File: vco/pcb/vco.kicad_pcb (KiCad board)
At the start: 2 copper layers, 50.5 x 108.5 mm, 98 parts, among them J1 Conn_02x05_Odd_Even, J10 AudioJack2_SwitchT, J2 AudioJack2_SwitchT, J3 AudioJack2_SwitchT, J4 AudioJack2_SwitchT, J5 AudioJack2_SwitchT, J6 AudioJack2_SwitchT, J7 AudioJack2_SwitchT, J8 AudioJack2_SwitchT, J9 AudioJack2_SwitchT, Q1 DMMT3906W, Q2 BC847, SW1 SW_SPDT, SW2 SW_SPDT, U1 TL072, U2 TL074, U3 LM13700, U4 ICM7555xB, U5 TL074

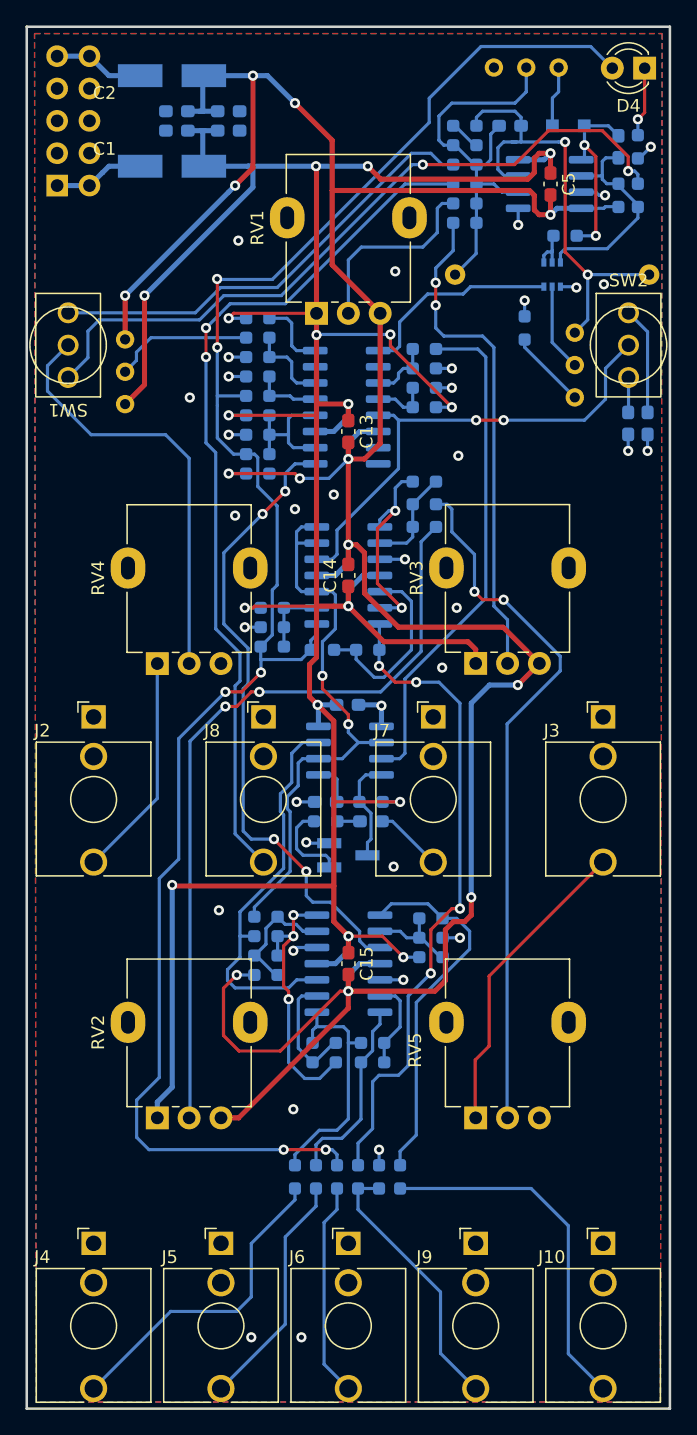
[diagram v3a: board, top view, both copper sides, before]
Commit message: vco: Organize component markings
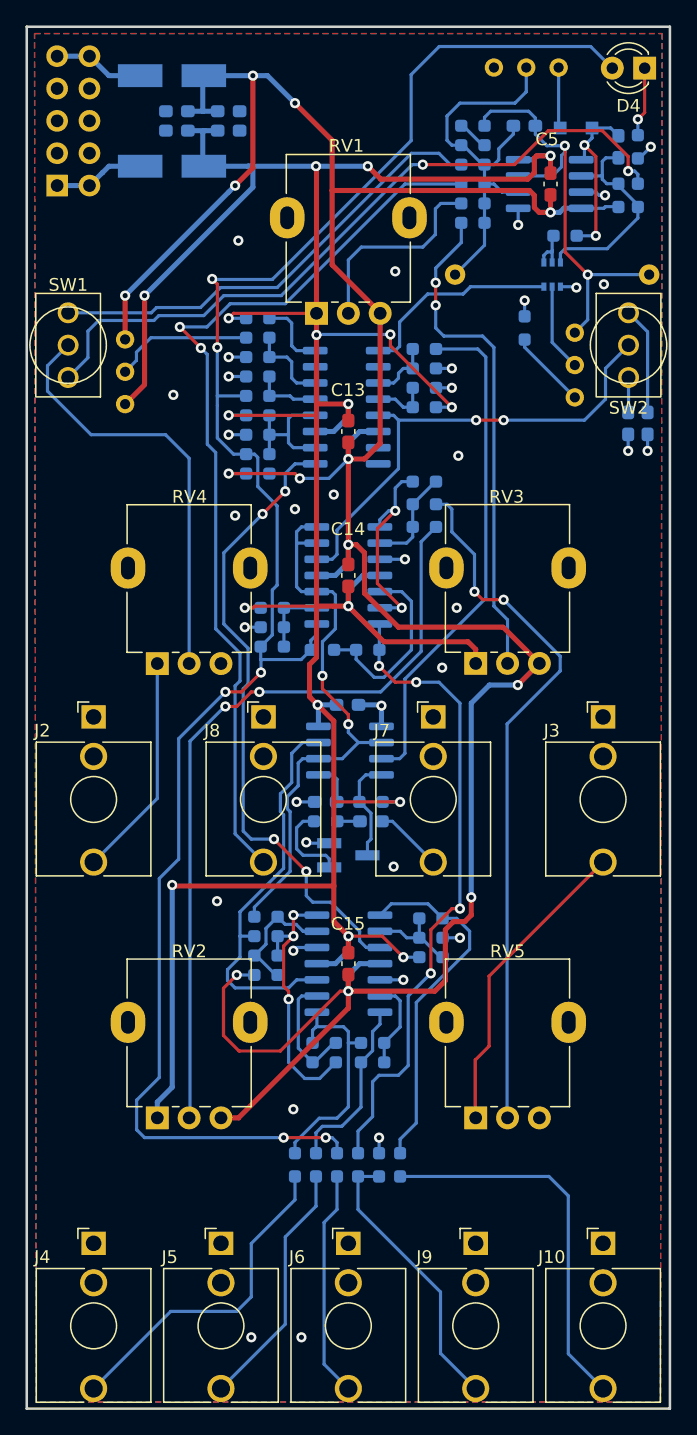
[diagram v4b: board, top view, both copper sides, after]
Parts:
- moved C6 1.12 mm to (154.2, 59.3)
- moved R22 0.95 mm to (139.5, 140.8)
- moved R32 0.95 mm to (141.1, 140.8)
- moved R33 0.95 mm to (142.8, 140.8)
- moved R45 0.95 mm to (144.4, 140.8)
- moved R52 0.95 mm to (137.8, 140.8)
- moved R53 0.95 mm to (136.2, 140.8)
- moved D3 0.64 mm to (158.2, 59.4)
- moved R1 0.63 mm to (150.1, 65.4)
- moved R2 0.63 mm to (150.1, 66.9)
- moved R3 0.63 mm to (150.1, 63.8)
- moved R4 0.63 mm to (150.1, 62.3)
- moved R5 0.63 mm to (150.1, 60.8)
- moved R7 0.63 mm to (150.1, 59.3)
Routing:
- net CVJack: track 68.2 -> 71.8 mm
- net Sine: track 28.3 -> 30.1 mm
- net Net-(C6-Pad2): track 36.9 -> 35.2 mm
- net Net-(D4-Pad2): track 141.9 -> 143.7 mm
- net Net-(R49-Pad1): track 19.3 -> 18.3 mm
- net Net-(R42-Pad1): track 28.8 -> 27.9 mm
- net Net-(R24-Pad2): track 51.7 -> 50.8 mm
- net Net-(R51-Pad2): track 15.0 -> 14.0 mm
- net Tri: track 16.9 -> 17.9 mm
- net Square: track 21.2 -> 22.1 mm
- net SawInv: track 18.8 -> 19.7 mm
- net Saw: track 25.3 -> 26.2 mm
- net Net-(C6-Pad1): track 32.3 -> 31.5 mm
- net -12V: track 223.6 -> 222.9 mm
- net FCPot: track 15.4 -> 16.1 mm
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
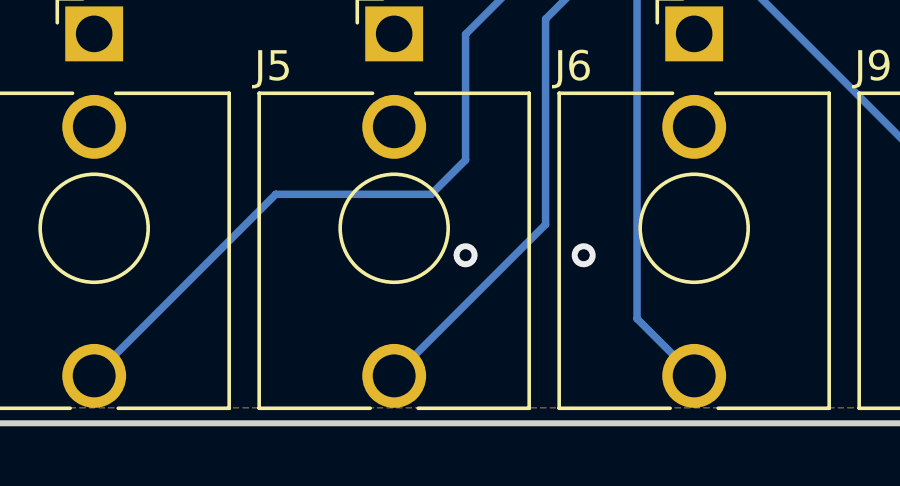
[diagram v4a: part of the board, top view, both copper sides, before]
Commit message: vco: Add the project name on the PCB
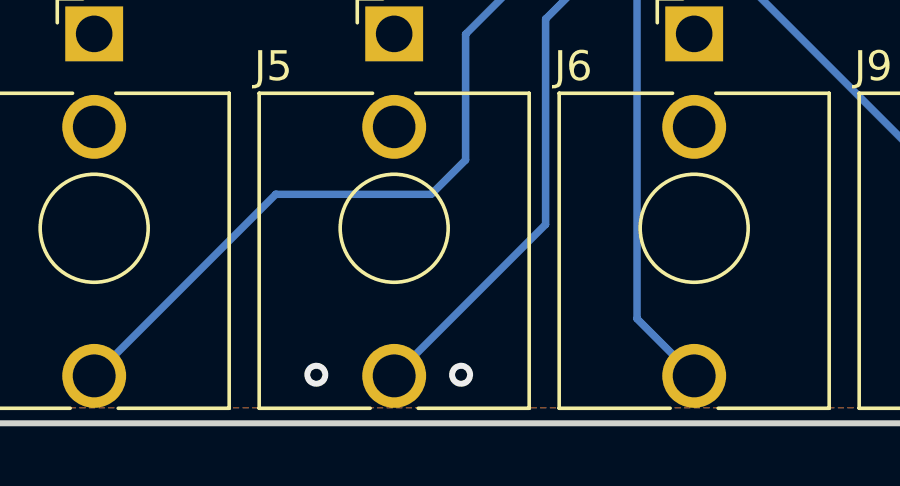
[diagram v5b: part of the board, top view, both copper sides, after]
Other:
- board text added: "(VC|LF)O Rev. 1 2022"
- board text added: "L. Rittel"
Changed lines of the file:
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@@
   (gr_rect locked (start 115.108 41.486295) (end 165.608 169.986295) (layer "Dwgs.User") (width 0.2) (fill none))
   (gr_rect locked (start 115.108 51.486295) (end 165.608 159.986295) (layer "Edge.Cuts") (width 0.2) (fill none))
+  (gr_text "L. Rittel" (at 121.285 153.924) (layer "B.SilkS")
+    (effects (font (size 1.5 1.5) (thickness 0.3)) (justify mirror))
+  )
+  (gr_text "(VC|LF)O Rev. 1 2022" (at 148.971 153.797) (layer "B.SilkS")
+    (effects (font (size 1.5 1.5) (thickness 0.3)) (justify mirror))
+  )
   (dimension (type aligned) (layer "Dwgs.User")
     (pts (xy 115.358 41.736295) (xy 115.358 170.236295))
@@
   (via (at 131.468 89.869295) (size 0.8) (drill 0.4) (layers "F.Cu" "B.Cu") (free) (net 2))
   (via (at 131.722 68.279295) (size 0.8) (drill 0.4) (layers "F.Cu" "B.Cu") (free) (net 2))
-  (via (at 132.738 154.385295) (size 0.8) (drill 0.4) (layers "F.Cu" "B.Cu") (free) (net 2))
+  (via (at 127.762 158.369) (size 0.8) (drill 0.4) (layers "F.Cu" "B.Cu") (free) (net 2))
   (via (at 154.201 72.978295) (size 0.8) (drill 0.4) (layers "F.Cu" "B.Cu") (net 2))
   (via (at 142.771 138.7075) (size 0.8) (drill 0.4) (layers "F.Cu" "B.Cu") (net 2))
@@
   (via (at 164.107 60.913295) (size 0.8) (drill 0.4) (layers "F.Cu" "B.Cu") (net 2))
   (via (at 158.265 71.962295) (size 0.8) (drill 0.4) (layers "F.Cu" "B.Cu") (net 2))
-  (via (at 136.675 154.385295) (size 0.8) (drill 0.4) (layers "F.Cu" "B.Cu") (free) (net 2))
+  (via (at 132.588 158.369) (size 0.8) (drill 0.4) (layers "F.Cu" "B.Cu") (free) (net 2))
   (via (at 132.23 98.632295) (size 0.8) (drill 0.4) (layers "F.Cu" "B.Cu") (net 2))
   (via (at 130.048 120.142) (size 0.8) (drill 0.4) (layers "F.Cu" "B.Cu") (free) (net 2))

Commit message: vco: Add Mouser order codes
Add Mouser order codes to some parts.  THis solution isn't really nice, though.
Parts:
- D1, D2: value D_Schottky -> B130-13F
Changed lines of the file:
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@@
     (descr "LED, Round, FlatTop, diameter 3.0mm, 2 pins, http://www.kingbright.com/attachments/file/psearch/000/00/00/L-47XEC(Ver.9A).pdf")
     (tags "LED Round FlatTop diameter 3.0mm 2 pins")
+    (property "Mouser" " 604-WP424IDT ")
     (property "Sheetfile" "oscillator.kicad_sch")
     (property "Sheetname" "Oscillator")
@@
     (descr "SOIC, 8 Pin (JEDEC MS-012AA, https://www.analog.com/media/en/package-pcb-resources/package/pkg_pdf/soic_narrow-r/r_8.pdf), generated with kicad-footprint-generator ipc_gullwing_generator.py")
     (tags "SOIC SO")
+    (property "Mouser" " 968-ICM7555IBAZ-T ")
     (property "Sheetfile" "oscillator.kicad_sch")
     (property "Sheetname" "Oscillator")
@@
     (descr "SOD-323")
     (tags "SOD-323")
+    (property "Mouser" " 512-1N4148WS ")
     (property "Sheetfile" "connectors_supply_exponentiation.kicad_sch")
     (property "Sheetname" "Connectors, Supply and Exponentiation")
@@
     (descr "SOIC, 16 Pin (JEDEC MS-012AC, https://www.analog.com/media/en/package-pcb-resources/package/pkg_pdf/soic_narrow-r/r_16.pdf), generated with kicad-footprint-generator ipc_gullwing_generator.py")
     (tags "SOIC SO")
+    (property "Mouser" " 926-LM13700MX/NOPB ")
     (property "Sheetfile" "oscillator.kicad_sch")
     (property "Sheetname" "Oscillator")
@@
     (descr "SOIC, 8 Pin (JEDEC MS-012AA, https://www.analog.com/media/en/package-pcb-resources/package/pkg_pdf/soic_narrow-r/r_8.pdf), generated with kicad-footprint-generator ipc_gullwing_generator.py")
     (tags "SOIC SO")
+    (property "Mouser" "595-TL072CDR ")
     (property "Sheetfile" "connectors_supply_exponentiation.kicad_sch")
     (property "Sheetname" "Connectors, Supply and Exponentiation")
@@
     (descr "SOIC, 14 Pin (JEDEC MS-012AB, https://www.analog.com/media/en/package-pcb-resources/package/pkg_pdf/soic_narrow-r/r_14.pdf), generated with kicad-footprint-generator ipc_gullwing_generator.py")
     (tags "SOIC SO")
+    (property "Mouser" " 595-TL074CDR ")
     (property "Sheetfile" "oscillator.kicad_sch")
     (property "Sheetname" "Oscillator")
@@
     (descr "Diode SMA (DO-214AC) Handsoldering")
     (tags "Diode SMA (DO-214AC) Handsoldering")
+    (property "Mouser" " 621-B130-F ")
     (property "Sheetfile" "connectors_supply_exponentiation.kicad_sch")
     (property "Sheetname" "Connectors, Supply and Exponentiation")
@@
       (effects (font (size 1 1) (thickness 0.15)) (justify mirror))
     )
-    (fp_text value "D_Schottky" (at 0 -2.6 180) (layer "B.Fab")
+    (fp_text value "B130-13F" (at 0 -2.6 180) (layer "B.Fab")
       (effects (font (size 1 1) (thickness 0.15)) (justify mirror))
     )
@@
     (descr "Diode SMA (DO-214AC) Handsoldering")
     (tags "Diode SMA (DO-214AC) Handsoldering")
+    (property "Mouser" " 621-B130-F ")
     (property "Sheetfile" "connectors_supply_exponentiation.kicad_sch")
     (property "Sheetname" "Connectors, Supply and Exponentiation")
@@
       (effects (font (size 1 1) (thickness 0.15)) (justify mirror))
     )
-    (fp_text value "D_Schottky" (at 0 -2.6) (layer "B.Fab")
+    (fp_text value "B130-13F" (at 0 -2.6) (layer "B.Fab")
       (effects (font (size 1 1) (thickness 0.15)) (justify mirror))
     )
@@
     (descr "SOT-363, SC-70-6")
     (tags "SOT-363 SC-70-6")
+    (property "Mouser" " 621-DMMT3906W-F ")
     (property "Sheetfile" "connectors_supply_exponentiation.kicad_sch")
     (property "Sheetname" "Connectors, Supply and Exponentiation")
@@
     (descr "SOIC, 14 Pin (JEDEC MS-012AB, https://www.analog.com/media/en/package-pcb-resources/package/pkg_pdf/soic_narrow-r/r_14.pdf), generated with kicad-footprint-generator ipc_gullwing_generator.py")
     (tags "SOIC SO")
+    (property "Mouser" " 595-TL074CDR ")
     (property "Sheetfile" "oscillator.kicad_sch")
     (property "Sheetname" "Oscillator")
@@
     (descr "Through hole straight pin header, 2x05, 2.54mm pitch, double rows")
     (tags "Through hole pin header THT 2x05 2.54mm double row")
+    (property "Mouser" " 200-TSW10507GD ")
     (property "Sheetfile" "connectors_supply_exponentiation.kicad_sch")
     (property "Sheetname" "Connectors, Supply and Exponentiation")
@@
     (descr "SOT-23, Handsoldering")
     (tags "SOT-23")
+    (property "Mouser" " 771-BC847C-T/R ")
     (property "Sheetfile" "oscillator.kicad_sch")
     (property "Sheetname" "Oscillator")

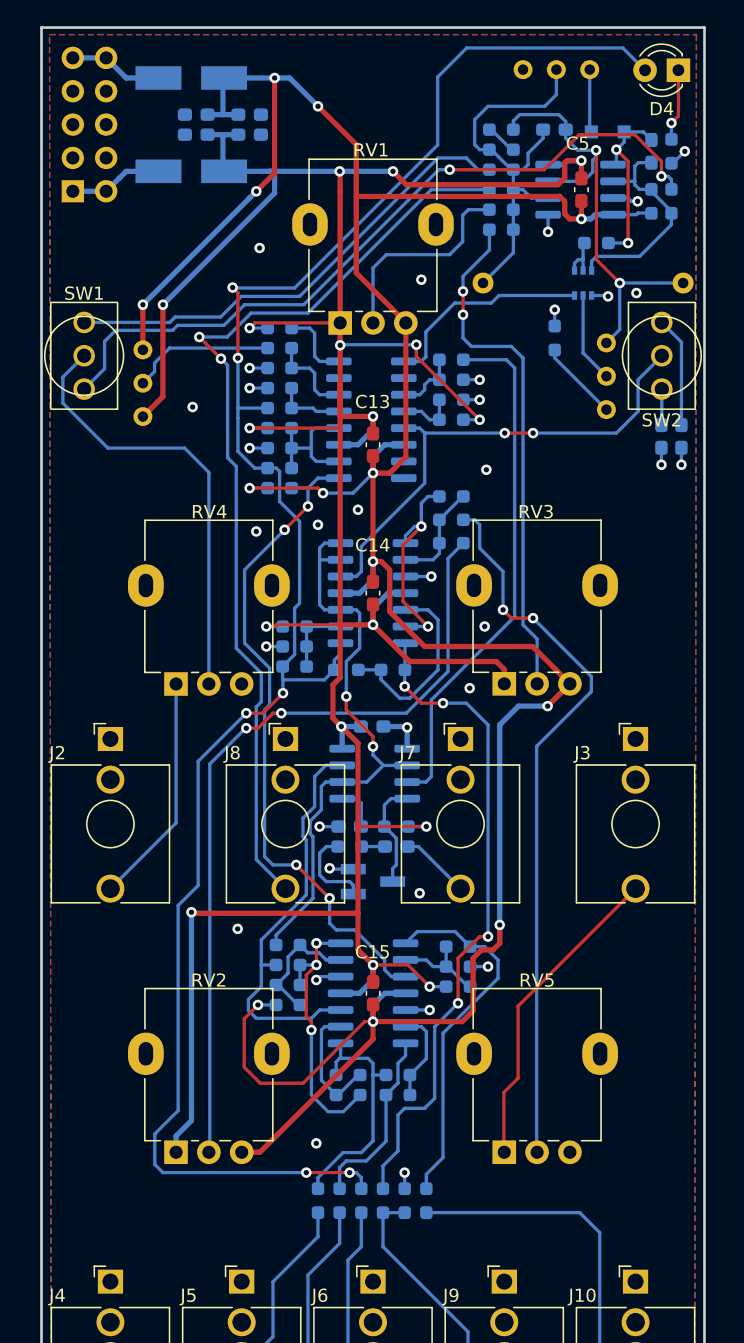
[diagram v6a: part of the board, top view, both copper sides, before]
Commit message: vco: Add more info to silk
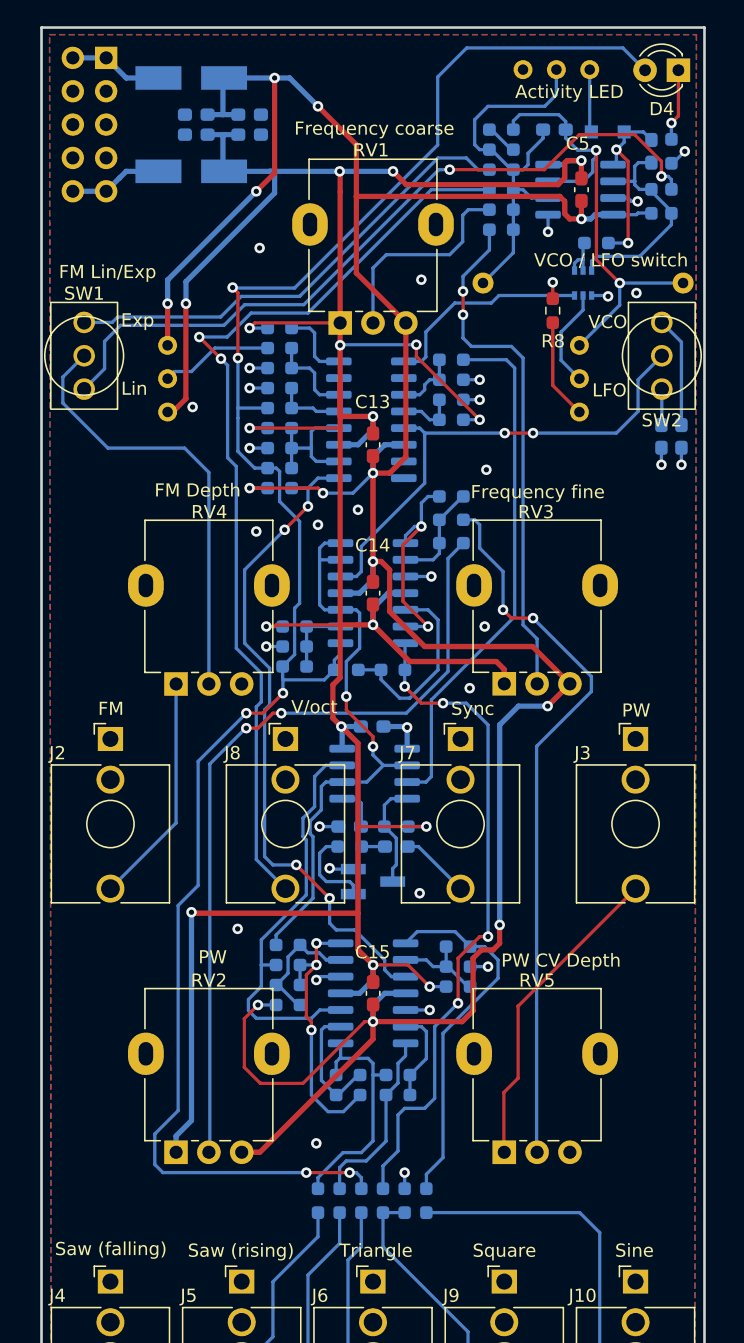
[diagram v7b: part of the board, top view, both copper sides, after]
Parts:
- R8: moved to F.Cu
- moved J1 10.5 mm to (120.0, 53.8), turned to 180 degrees
- moved R8 2.09 mm to (154.1, 73.0)
- moved RV6 2.06 mm to (156.1, 75.7)
- moved RV8 1.91 mm to (124.7, 80.8)
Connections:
- J1 pad 1: Net-(D1-Pad2) -> Net-(D2-Pad1)
- J1 pad 10: Net-(D2-Pad1) -> Net-(D1-Pad2)
- J1 pad 2: Net-(D1-Pad2) -> Net-(D2-Pad1)
- J1 pad 9: Net-(D2-Pad1) -> Net-(D1-Pad2)
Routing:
- net Net-(R26-Pad1): track 11.0 -> 8.59 mm
- net Net-(R8-Pad1): track 6.17 -> 7.65 mm
- net -12V: track 222.9 -> 221.7 mm
- net Net-(C6-Pad2): track 35.2 -> 36.2 mm
- net +12V: track 246.0 -> 245.1 mm
- net Net-(Q1-Pad2): track 6.89 -> 7.61 mm
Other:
- board text added: "Activity LED"
- board text added: "Exp"
- board text added: "FM"
- board text added: "FM Depth"
- board text added: "FM Lin/Exp"
- board text added: "Frequency coarse"
- board text added: "Frequency fine"
- board text added: "HF adj"
- board text added: "LFO"
- board text added: "Lin"
- board text added: "PW"
- board text added: "PW CV Depth"
- board text added: "Saw (falling)"
- board text added: "Saw (rising)"
- board text added: "Sine"
- board text added: "Sine adj"
- board text added: "Square"
- board text added: "Sync"
- board text added: "Triangle"
- board text added: "V/oct"
- board text added: "V/oct adj"
- board text added: "VCO"
- board text added: "VCO / LFO switch"
